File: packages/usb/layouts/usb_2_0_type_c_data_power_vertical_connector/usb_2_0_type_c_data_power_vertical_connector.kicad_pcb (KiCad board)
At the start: 2 copper layers, 6 parts

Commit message: WIP update usb
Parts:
- C1: footprint atopile:C0402-b3ef17 -> Samsung_Electro_Mechanics_CL05B104KO5NNNC:C0402
- R1, R2: footprint atopile:R0402-56259e -> UNI_ROYAL_0402WGF5101TCE:R0402
- U1: footprint atopile:SOT-23-6_L2.9-W1.6-P0.95-LS2.8-BL-d2c740 -> TECH_PUBLIC_USBLC6_2SC6:SOT-23-6_L2.9-W1.6-P0.95-LS2.8-BL
- U2: footprint atopile:F0805-d5954a -> BHFUSE_BSMD0805_050_15V:F0805
- X1: footprint atopile:USB-C-TH_TYPE-C-USB-14P-1a34cb -> Jing_Extension_of_the_Electronic_Co_918_418K2022Y40000:USB-C-TH_TYPE-C-USB-14P
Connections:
- C1 pad 1: hv-1 -> hv
- U1 pad 5: hv-1 -> hv
- U2 pad 1: hv -> hv-1
- U2 pad 2: hv-1 -> hv
- X1 pad 13: hv -> hv-1
- X1 pad 2: hv -> hv-1
- X1 pad 6: hv -> hv-1
- X1 pad 9: hv -> hv-1
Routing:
- net hv-1: track 12.2 -> 25.9 mm, vias 3 -> 1
- net hv: track 25.9 -> 12.2 mm, vias 1 -> 3

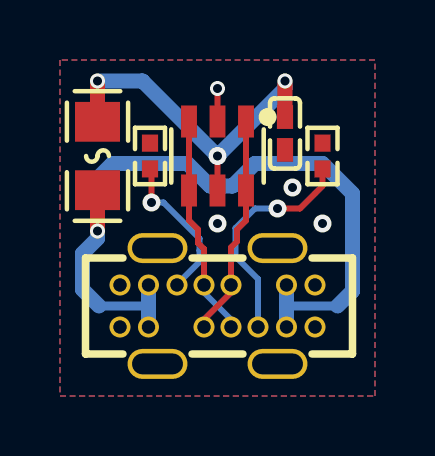
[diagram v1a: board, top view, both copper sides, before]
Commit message: Manually fix fp lib tables
fix some small bugs
fix package only modules (e.g. logos)
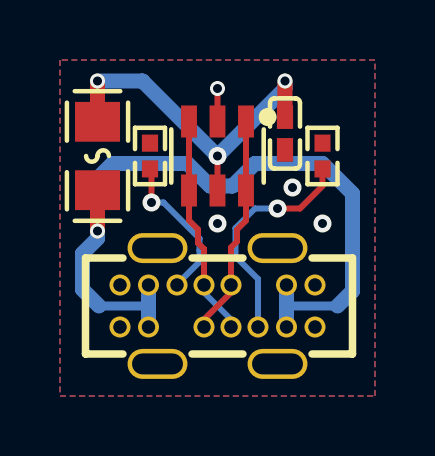
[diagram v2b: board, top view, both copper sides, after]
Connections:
- C1 pad 1: hv -> hv-1
- R1 pad 1: line-3 -> line-2
- R2 pad 1: line-1 -> line-3
- U1 pad 1: line-2 -> line-1
- U1 pad 5: hv -> hv-1
- U1 pad 6: line-2 -> line-1
- U2 pad 1: hv-1 -> hv
- U2 pad 2: hv -> hv-1
- X1 pad 10: line-2 -> line-1
- X1 pad 12: line-3 -> line-2
- X1 pad 13: hv-1 -> hv
- X1 pad 2: hv-1 -> hv
- X1 pad 3: line-2 -> line-1
- X1 pad 5: line-1 -> line-3
- X1 pad 6: hv-1 -> hv
- X1 pad 9: hv-1 -> hv
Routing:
- net hv-1: track 25.9 -> 12.2 mm, vias 1 -> 3
- net hv: track 12.2 -> 25.9 mm, vias 3 -> 1
- net line-3: track 5.10 -> 7.66 mm
- net line-2: track 7.43 -> 5.10 mm, vias 0 -> 1
- net line-1: track 7.66 -> 7.43 mm, vias 1 -> 0

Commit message: rebuild all packages & regenerate images of changed layouts (silk)
Add new scripts for version bump and build (based on atopile/packages)
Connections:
- R1 pad 1: line-2 -> line
- R2 pad 1: line-3 -> line-1
- U1 pad 1: line-1 -> line-2
- U1 pad 3: line -> line-3
- U1 pad 4: line -> line-3
- U1 pad 6: line-1 -> line-2
- X1 pad 10: line-1 -> line-2
- X1 pad 11: line -> line-3
- X1 pad 12: line-2 -> line
- X1 pad 3: line-1 -> line-2
- X1 pad 4: line -> line-3
- X1 pad 5: line-3 -> line-1
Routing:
- net line-2: track 5.10 -> 7.43 mm, vias 1 -> 0
- net line: track 7.43 -> 5.10 mm, vias 0 -> 1
- net line-3: track 7.66 -> 7.43 mm, vias 1 -> 0
- net line-1: track 7.43 -> 7.66 mm, vias 0 -> 1
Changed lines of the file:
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@@
     (net 1 "hv-1")
     (net 2 "gnd")
-    (net 3 "line-2")
-    (net 4 "line")
-    (net 5 "line-3")
+    (net 3 "line")
+    (net 4 "line-3")
+    (net 5 "line-1")
     (net 6 "hv")
-    (net 7 "line-1")
+    (net 7 "line-2")
     (footprint "Samsung_Electro_Mechanics_CL05B104KO5NNNC:C0402"
         (layer "F.Cu")
@@
             (size 0.53 1.07)
             (layers "F.Cu" "F.Paste" "F.Mask")
-            (net 7 "line-1")
+            (net 7 "line-2")
         )
         (pad "2" smd rect
@@
             (size 0.53 1.07)
             (layers "F.Cu" "F.Paste" "F.Mask")
-            (net 4 "line")
+            (net 4 "line-3")
         )
         (pad "4" smd rect
@@
             (size 0.53 1.07)
             (layers "F.Cu" "F.Paste" "F.Mask")
-            (net 4 "line")
+            (net 4 "line-3")
         )
         (pad "5" smd rect
@@
             (size 0.53 1.07)
             (layers "F.Cu" "F.Paste" "F.Mask")
-            (net 7 "line-1")
+            (net 7 "line-2")
         )
         (model "${KIPRJMOD}/../../parts/TECH_PUBLIC_USBLC6_2SC6/SOT-23-6_L2.9-W1.6-H1.5-LS2.8-P0.95.step"
@@
             (drill 0.4499864)
             (layers "*.Cu" "*.Mask")
-            (net 7 "line-1")
+            (net 7 "line-2")
         )
         (pad "4" thru_hole circle
@@
             (drill 0.4499864)
             (layers "*.Cu" "*.Mask")
-            (net 4 "line")
+            (net 4 "line-3")
         )
         (pad "5" thru_hole circle
@@
             (drill 0.4499864)
             (layers "*.Cu" "*.Mask")
-            (net 5 "line-3")
+            (net 5 "line-1")
         )
         (pad "6" thru_hole circle
@@
             (drill 0.4499864)
             (layers "*.Cu" "*.Mask")
-            (net 7 "line-1")
+            (net 7 "line-2")
         )
         (pad "11" thru_hole circle
@@
             (drill 0.4499864)
             (layers "*.Cu" "*.Mask")
-            (net 4 "line")
+            (net 4 "line-3")
         )
         (pad "12" thru_hole circle
@@
             (drill 0.4499864)
             (layers "*.Cu" "*.Mask")
-            (net 3 "line-2")
+            (net 3 "line")
         )
         (pad "13" thru_hole circle
@@
             (size 0.57 0.54)
             (layers "F.Cu" "F.Paste" "F.Mask")
-            (net 3 "line-2")
+            (net 3 "line")
         )
         (model "${KIPRJMOD}/../../parts/UNI_ROYAL_0402WGF5101TCE/R0402_L1.0-W0.5-H0.4.step"
@@
             (size 0.57 0.54)
             (layers "F.Cu" "F.Paste" "F.Mask")
-            (net 5 "line-3")
+            (net 5 "line-1")
         )
         (model "${KIPRJMOD}/../../parts/UNI_ROYAL_0402WGF5101TCE/R0402_L1.0-W0.5-H0.4.step"

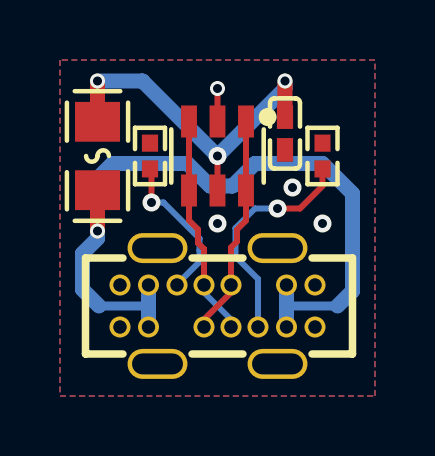
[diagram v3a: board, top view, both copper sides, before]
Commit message: Use packages from packages folder
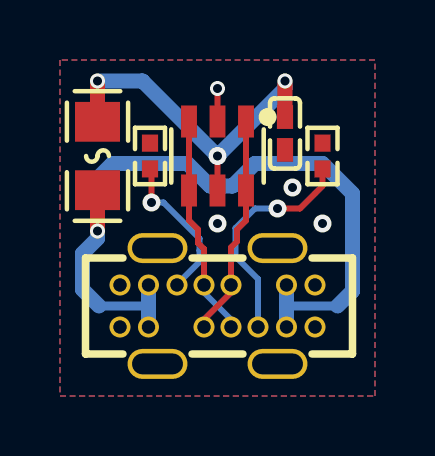
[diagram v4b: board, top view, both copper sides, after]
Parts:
- removed U2: , BHFUSE_BSMD0805_050_15V:F0805
- added F1: , BHFUSE_BSMD0805_050_15V:F0805, F.Cu at (-4.00, -5.75)
